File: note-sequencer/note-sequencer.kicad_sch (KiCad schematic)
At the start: 94 parts, among them J1 Pitch, J2 Gate, J3 Velocity, J4 Clock, J5 Power, J6 Power, J7 Power, SW1 C1, SW10 A1, SW11 A#1, SW12 B1, SW13 C2, SW14 C#2, SW15 D2, SW16 D#2, SW17 E2, SW18 F2, SW19 F#2, SW2 C#1, SW20 G2, SW21 G#2, SW22 A2, SW23 A#2, SW24 B2, SW25 C3, SW26 X1, SW27 X2, SW28 X3, SW29 X4, SW3 D1, SW31 RotaryEncoder_Switch, SW32 C2, SW33 Clock Source, SW34 SW_DIP_x01, SW35 Mode, SW4 D#1, SW5 E1, SW6 F1, SW7 F#1, SW8 G1, SW9 G#1, U4 TL072

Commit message: Update note sequencer
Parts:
- removed C4: 100nf, Capacitor_THT:C_Disc_D4.3mm_W1.9mm_P5.00mm, symbol Device:C_Small
- added J10: Velocity, modular2:banana-jack, symbol Connector:Conn_01x01_Pin
- added J11: Pitch, modular2:banana-jack, symbol Connector:Conn_01x01_Pin
- added J12: Clock, modular2:banana-jack, symbol Connector:Conn_01x01_Pin
- added J13: Gate, modular2:banana-jack, symbol Connector:Conn_01x01_Pin
- added J14: LED Socket, Connector_PinHeader_2.54mm:PinHeader_1x02_P2.54mm_Vertical, symbol Connector:Conn_01x02_Socket
- added J8: Conn_01x06_Socket, Connector_PinSocket_2.54mm:PinSocket_1x06_P2.54mm_Vertical, symbol Connector:Conn_01x06_Socket
- added J9: Conn_01x06_Pin, Connector_PinHeader_2.54mm:PinHeader_1x06_P2.54mm_Vertical, symbol Connector:Conn_01x06_Pin
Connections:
- net at J4.1 (Pin_1), R7.2: now also J8.4 (Pin_4)
- net at J3.1 (Pin_1), R6.1: now also J8.3 (Pin_3)
- net at J1.1 (Pin_1), R5.1: now also J8.1 (Pin_1)
- net at A1.1 (D1/TX), D32.2 (A), R8.1: now also J8.5 (Pin_5)
- net at D32.1 (K), R9.2: now also J8.6 (Pin_6)
- net at J2.1 (Pin_1), R8.2: now also J8.2 (Pin_2)
- new net: J11.1 (Pin_1), J9.1 (Pin_1)
- new net: J12.1 (Pin_1), J9.2 (Pin_2)
- new net: J10.1 (Pin_1), J9.3 (Pin_3)
- new net: J13.1 (Pin_1), J9.4 (Pin_4)
- new net: J14.1 (Pin_1), J9.5 (Pin_5)
- new net: J14.2 (Pin_2), J9.6 (Pin_6)
- no-connect marks 33 -> 34
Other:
- moved on the sheet: J4, R7

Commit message: Updates
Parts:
- added SW30: SW_DIP_x01, Button_Switch_THT:SW_DIP_SPSTx01_Slide_9.78x4.72mm_W7.62mm_P2.54mm, symbol Switch:SW_DIP_x01
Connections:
- net at U1.11 (Lite): now also SW30.1; no longer A2.5 (D2)
- new net: A2.5 (D2), SW30.2
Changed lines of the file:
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@@
+	(wire
+		(pts
+			(xy 71.12 86.36) (xy 71.12 140.97)
+		)
+		(stroke
+			(width 0)
+			(type default)
+		)
+	)
 	(wire
 		(pts
@@
 	(wire
 		(pts
-			(xy 71.12 71.12) (xy 71.12 140.97)
-		)
-		(stroke
-			(width 0)
-			(type default)
-		)
-	)
-	(wire
-		(pts
 			(xy 172.72 92.71) (xy 196.85 92.71)
 		)
@@
 	(wire
 		(pts
+			(xy 71.12 86.36) (xy 73.66 86.36)
+		)
+		(stroke
+			(width 0)
+			(type default)
+		)
+	)
+	(wire
+		(pts
 			(xy 64.77 128.27) (xy 82.55 128.27)
 		)
@@
 	(wire
 		(pts
-			(xy 62.23 71.12) (xy 71.12 71.12)
+			(xy 62.23 71.12) (xy 73.66 71.12)
 		)
 		(stroke
@@
 					(unit 1)
 				)
+			)
+		)
+	)
+	(symbol
+		(lib_id "Switch:SW_DIP_x01")
+		(at 73.66 78.74 90)
+		(unit 1)
+		(exclude_from_sim no)
+		(in_bom yes)
+		(on_board yes)
+		(dnp no)
+		(fields_autoplaced yes)
+		(property "Reference" "SW30"
+			(at 77.47 77.4699 90)
+			(effects
+				(font
+					(size 1.27 1.27)
+				)
+				(justify right)
+			)
+		)
+		(property "Value" "SW_DIP_x01"
+			(at 77.47 80.0099 90)
+			(effects
+				(font
+					(size 1.27 1.27)
+				)
+				(justify right)
+			)
+		)
+		(property "Footprint" "Button_Switch_THT:SW_DIP_SPSTx01_Slide_9.78x4.72mm_W7.62mm_P2.54mm"
+			(at 73.66 78.74 0)
+			(effects
+				(font
+					(size 1.27 1.27)
+				)
+				(hide yes)
+			)
+		)
+		(property "Datasheet" "~"
+			(at 73.66 78.74 0)
+			(effects
+				(font
+					(size 1.27 1.27)
+				)
+				(hide yes)
+			)
+		)
+		(property "Description" "1x DIP Switch, Single Pole Single Throw (SPST) switch, small symbol"
+			(at 73.66 78.74 0)
+			(effects
+				(font
+					(size 1.27 1.27)
+				)
+				(hide yes)
+			)
+		)
+		(pin "1"
+		)
+		(pin "2"
+		)
+		(instances
+			(project "note-sequencer"
+				(path "/f98772eb-f079-4488-8f73-e60cea43bd5f"
+					(reference "SW30")
+					(unit 1)
+				)

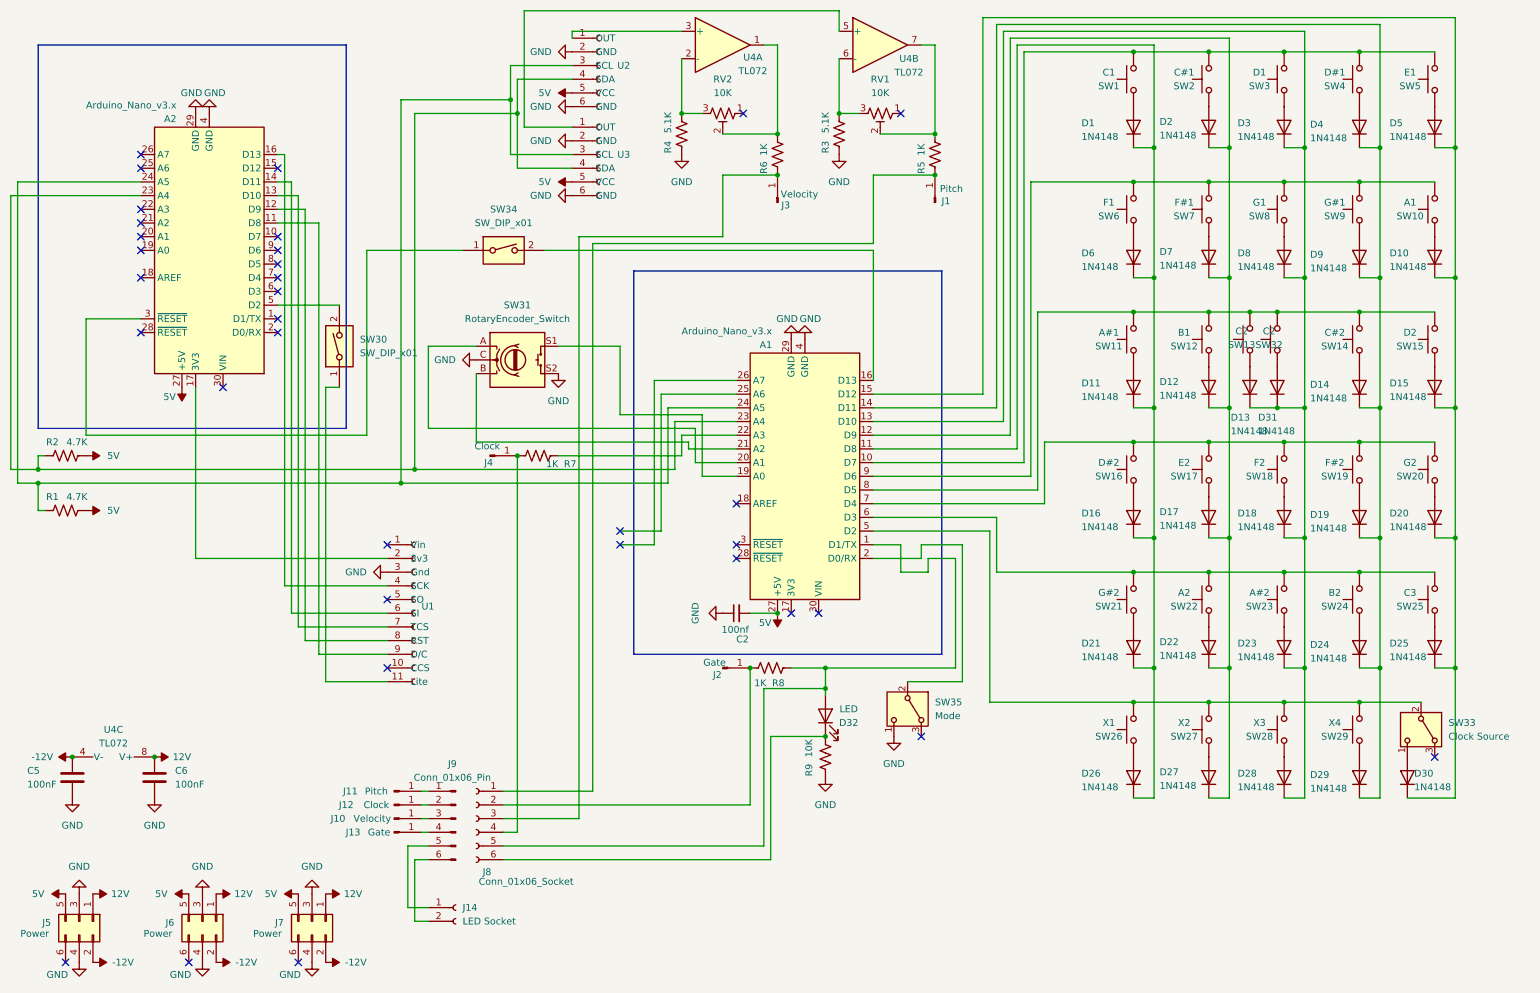
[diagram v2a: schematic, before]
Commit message: Renumber some components
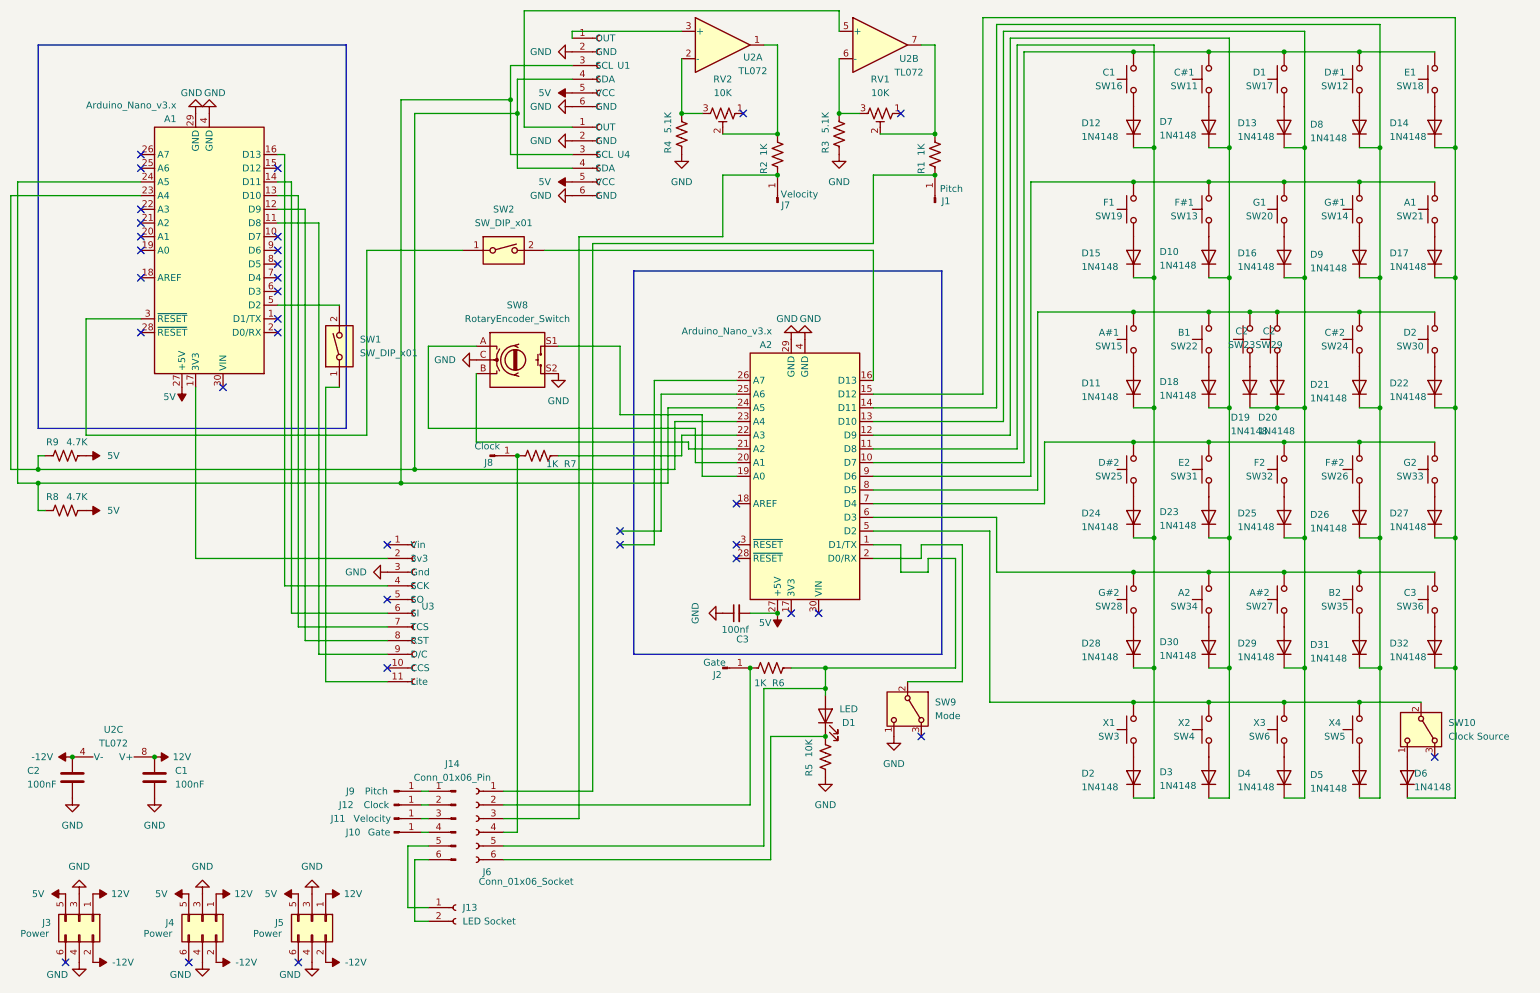
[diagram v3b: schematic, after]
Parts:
- renumbered A2 to A1, A1 to A2, C6 to C1, C5 to C2, C2 to C3, D32 to D1, D7 to D10, D1 to D12, D3 to D13, D5 to D14, D6 to D15, D8 to D16, D10 to D17, D12 to D18, D13 to D19, D26 to D2, D31 to D20, D14 to D21, D15 to D22, D17 to D23, D16 to D24, D18 to D25, D19 to D26, D20 to D27, D21 to D28, D23 to D29, D27 to D3, D22 to D30, D24 to D31, D25 to D32, D28 to D4, D29 to D5, D30 to D6, D2 to D7, D4 to D8, J13 to J10, J10 to J11, J14 to J13, J9 to J14, J5 to J3, J6 to J4, J7 to J5, J8 to J6, J3 to J7, J4 to J8, J11 to J9, R5 to R1, R6 to R2, R9 to R5, R8 to R6, R1 to R8, R2 to R9, SW30 to SW1, SW33 to SW10, SW2 to SW11, SW4 to SW12, SW7 to SW13, SW9 to SW14, SW11 to SW15, SW1 to SW16, SW3 to SW17, SW5 to SW18, SW6 to SW19, SW34 to SW2, SW8 to SW20, SW10 to SW21, SW12 to SW22, SW13 to SW23, SW14 to SW24, SW16 to SW25, SW19 to SW26, SW23 to SW27, SW21 to SW28, SW32 to SW29, SW26 to SW3, SW15 to SW30, SW17 to SW31, SW18 to SW32, SW20 to SW33, SW22 to SW34, SW24 to SW35, SW25 to SW36, SW27 to SW4, SW29 to SW5, SW28 to SW6, SW31 to SW8, SW35 to SW9, U2 to U1, U4 to U2, U1 to U3, U3 to U4

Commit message: Revert "Renumber some components"
This reverts commit 4c9a93e4336de2276d9b49e02718b6a92f997a6a.
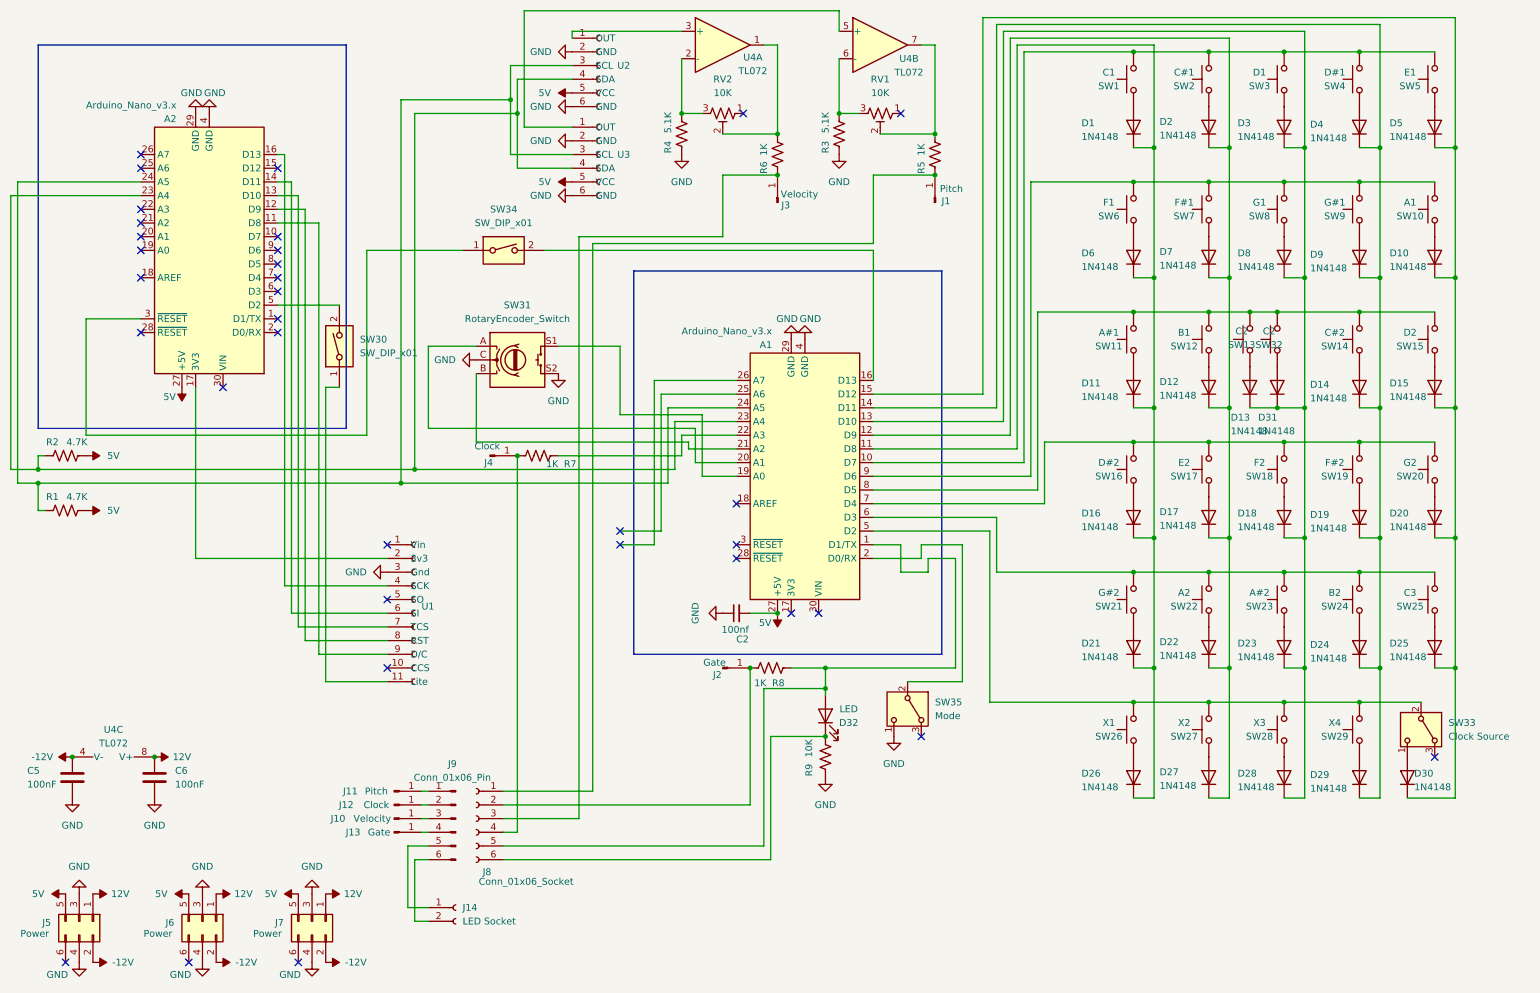
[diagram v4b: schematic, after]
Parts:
- renumbered A2 to A1, A1 to A2, C3 to C2, C2 to C5, C1 to C6, D12 to D1, D17 to D10, D18 to D12, D19 to D13, D21 to D14, D22 to D15, D24 to D16, D23 to D17, D25 to D18, D26 to D19, D7 to D2, D27 to D20, D28 to D21, D30 to D22, D29 to D23, D31 to D24, D32 to D25, D2 to D26, D3 to D27, D4 to D28, D5 to D29, D13 to D3, D6 to D30, D20 to D31, D1 to D32, D8 to D4, D14 to D5, D15 to D6, D10 to D7, D16 to D8, J11 to J10, J9 to J11, J10 to J13, J13 to J14, J7 to J3, J8 to J4, J3 to J5, J4 to J6, J5 to J7, J6 to J8, J14 to J9, R8 to R1, R9 to R2, R1 to R5, R2 to R6, R6 to R8, R5 to R9, SW16 to SW1, SW21 to SW10, SW15 to SW11, SW22 to SW12, SW23 to SW13, SW24 to SW14, SW30 to SW15, SW25 to SW16, SW31 to SW17, SW32 to SW18, SW26 to SW19, SW11 to SW2, SW33 to SW20, SW28 to SW21, SW34 to SW22, SW27 to SW23, SW35 to SW24, SW36 to SW25, SW3 to SW26, SW4 to SW27, SW6 to SW28, SW5 to SW29, SW17 to SW3, SW1 to SW30, SW8 to SW31, SW29 to SW32, SW10 to SW33, SW2 to SW34, SW9 to SW35, SW12 to SW4, SW18 to SW5, SW19 to SW6, SW13 to SW7, SW20 to SW8, SW14 to SW9, U3 to U1, U1 to U2, U4 to U3, U2 to U4

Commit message: More fixes
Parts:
- R6: renamed from R9; value 10K -> 1K
- renumbered A2 to A1, A1 to A2, C6 to C1, C5 to C2, C2 to C3, D32 to D1, D9 to D10, D1 to D12, D3 to D13, D5 to D14, D6 to D15, D8 to D16, D10 to D17, D12 to D18, D13 to D19, D30 to D2, D14 to D20, D31 to D21, D17 to D22, D16 to D23, D15 to D24, D18 to D25, D19 to D26, D21 to D27, D20 to D28, D22 to D29, D26 to D3, D23 to D30, D24 to D31, D25 to D32, D28 to D4, D27 to D5, D29 to D6, D2 to D7, D4 to D8, D7 to D9, J13 to J10, J10 to J11, J14 to J13, J9 to J14, J5 to J3, J6 to J4, J7 to J5, J8 to J6, J3 to J7, J4 to J8, J11 to J9, R3 to R1, R5 to R2, R6 to R3, R8 to R5, R1 to R8, R2 to R9, SW30 to SW1, SW2 to SW10, SW4 to SW11, SW7 to SW12, SW9 to SW13, SW11 to SW14, SW1 to SW15, SW3 to SW16, SW6 to SW17, SW5 to SW18, SW8 to SW19, SW34 to SW2, SW10 to SW20, SW12 to SW21, SW13 to SW22, SW14 to SW23, SW16 to SW24, SW19 to SW25, SW21 to SW26, SW23 to SW27, SW32 to SW28, SW15 to SW29, SW26 to SW3, SW17 to SW30, SW18 to SW31, SW20 to SW32, SW22 to SW33, SW24 to SW34, SW25 to SW35, SW27 to SW4, SW29 to SW5, SW28 to SW6, SW31 to SW7, SW35 to SW8, SW33 to SW9, U4 to U1, U1 to U3, U3 to U4

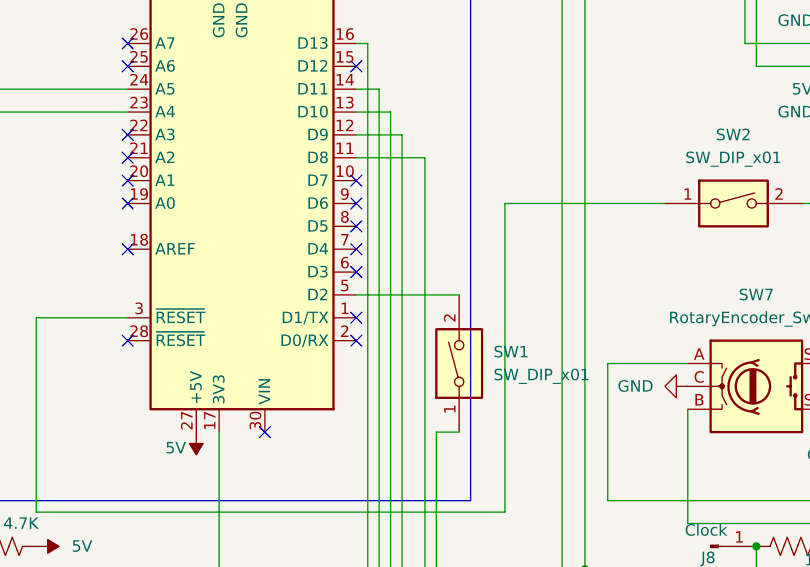
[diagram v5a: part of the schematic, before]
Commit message: Fix pwm pin controlling screen brightness
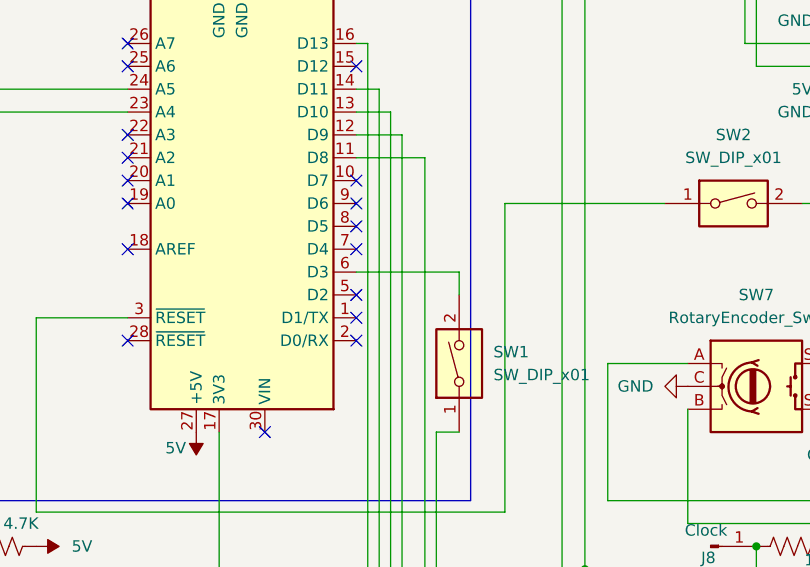
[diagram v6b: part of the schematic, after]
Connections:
- net at SW1.2: now also A1.6 (D3); no longer A1.5 (D2)
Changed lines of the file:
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@@
-	)
-	(no_connect
-		(at 62.23 68.58)
 	)
 	(no_connect
@@
 		(at 147.32 118.11)
 	)
+	(no_connect
+		(at 62.23 71.12)
+	)
 	(wire
 		(pts
@@
 	(wire
 		(pts
+			(xy 73.66 71.12) (xy 73.66 68.58)
+		)
+		(stroke
+			(width 0)
+			(type default)
+		)
+	)
+	(wire
+		(pts
 			(xy 62.23 53.34) (xy 67.31 53.34)
 		)
@@
 	(wire
 		(pts
+			(xy 73.66 68.58) (xy 62.23 68.58)
+		)
+		(stroke
+			(width 0)
+			(type default)
+		)
+	)
+	(wire
+		(pts
 			(xy 172.72 92.71) (xy 196.85 92.71)
 		)
@@
 		)
 		(stroke
-			(width 0)
-			(type default)
-		)
-	)
-	(wire
-		(pts
-			(xy 62.23 71.12) (xy 73.66 71.12)
-		)
-		(stroke

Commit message: Update some designs
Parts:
- U2, U3, U4: value ~ -> (none)
